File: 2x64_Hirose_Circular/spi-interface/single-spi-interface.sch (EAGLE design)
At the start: 53 parts, among them P1 BLUE, P2 BLUE, P3 BLUE, P4 BLUE, P5 BLUE, Q1 BC817, Q2 BC817

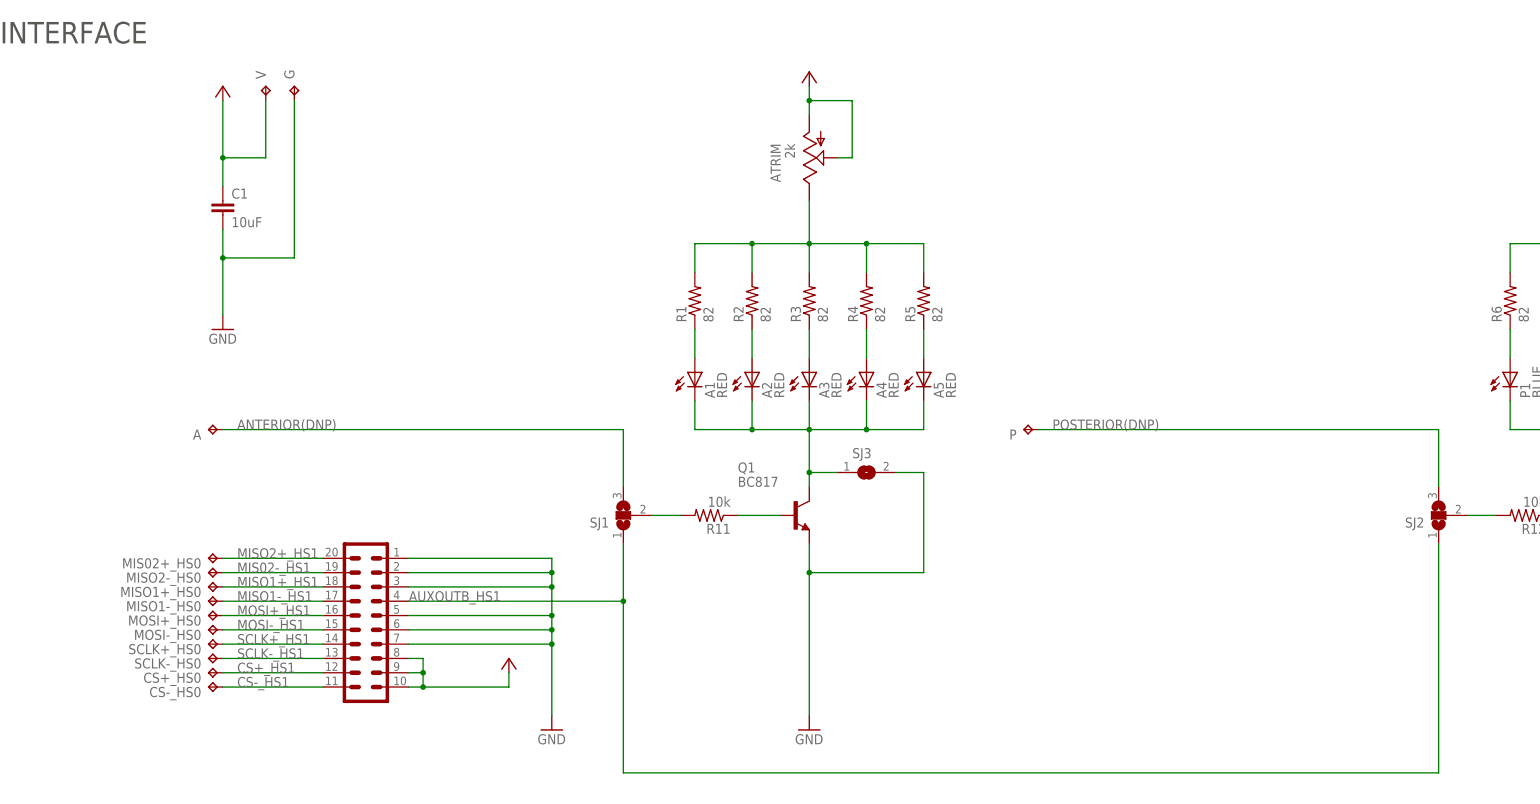
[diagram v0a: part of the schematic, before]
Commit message: Minor mods to headstage. Started routing the SPI interface.
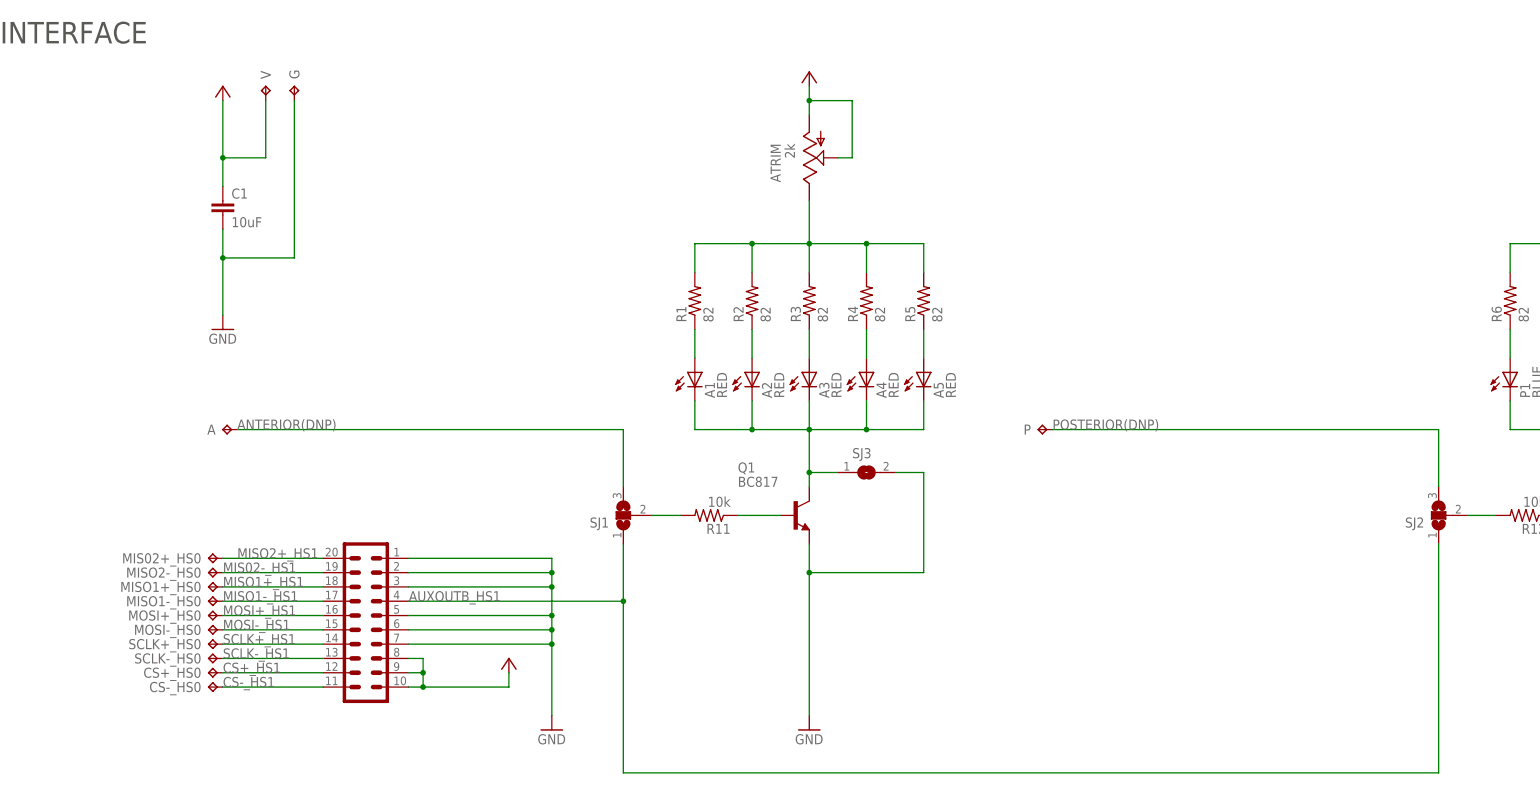
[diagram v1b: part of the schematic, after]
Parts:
- A, CS+_HS0, CS-_HS0, MIS02+_HS0, MISO1+_HS0, MISO1-_HS0, MISO2-_HS0, MOSI+_HS0, MOSI-_HS0, P, SCLK+_HS0, SCLK-_HS0: value TP_01 -> TP_SPI_WIRE; device headstage:TP_01 -> jonnew:TP_SPI_WIRE
- G, V: value TP_02 -> TP_SPI_WIRE; device headstage:TP_02 -> jonnew:TP_SPI_WIRE
- renumbered HS1 to DIO_HS0
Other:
- moved on the sheet: A, P

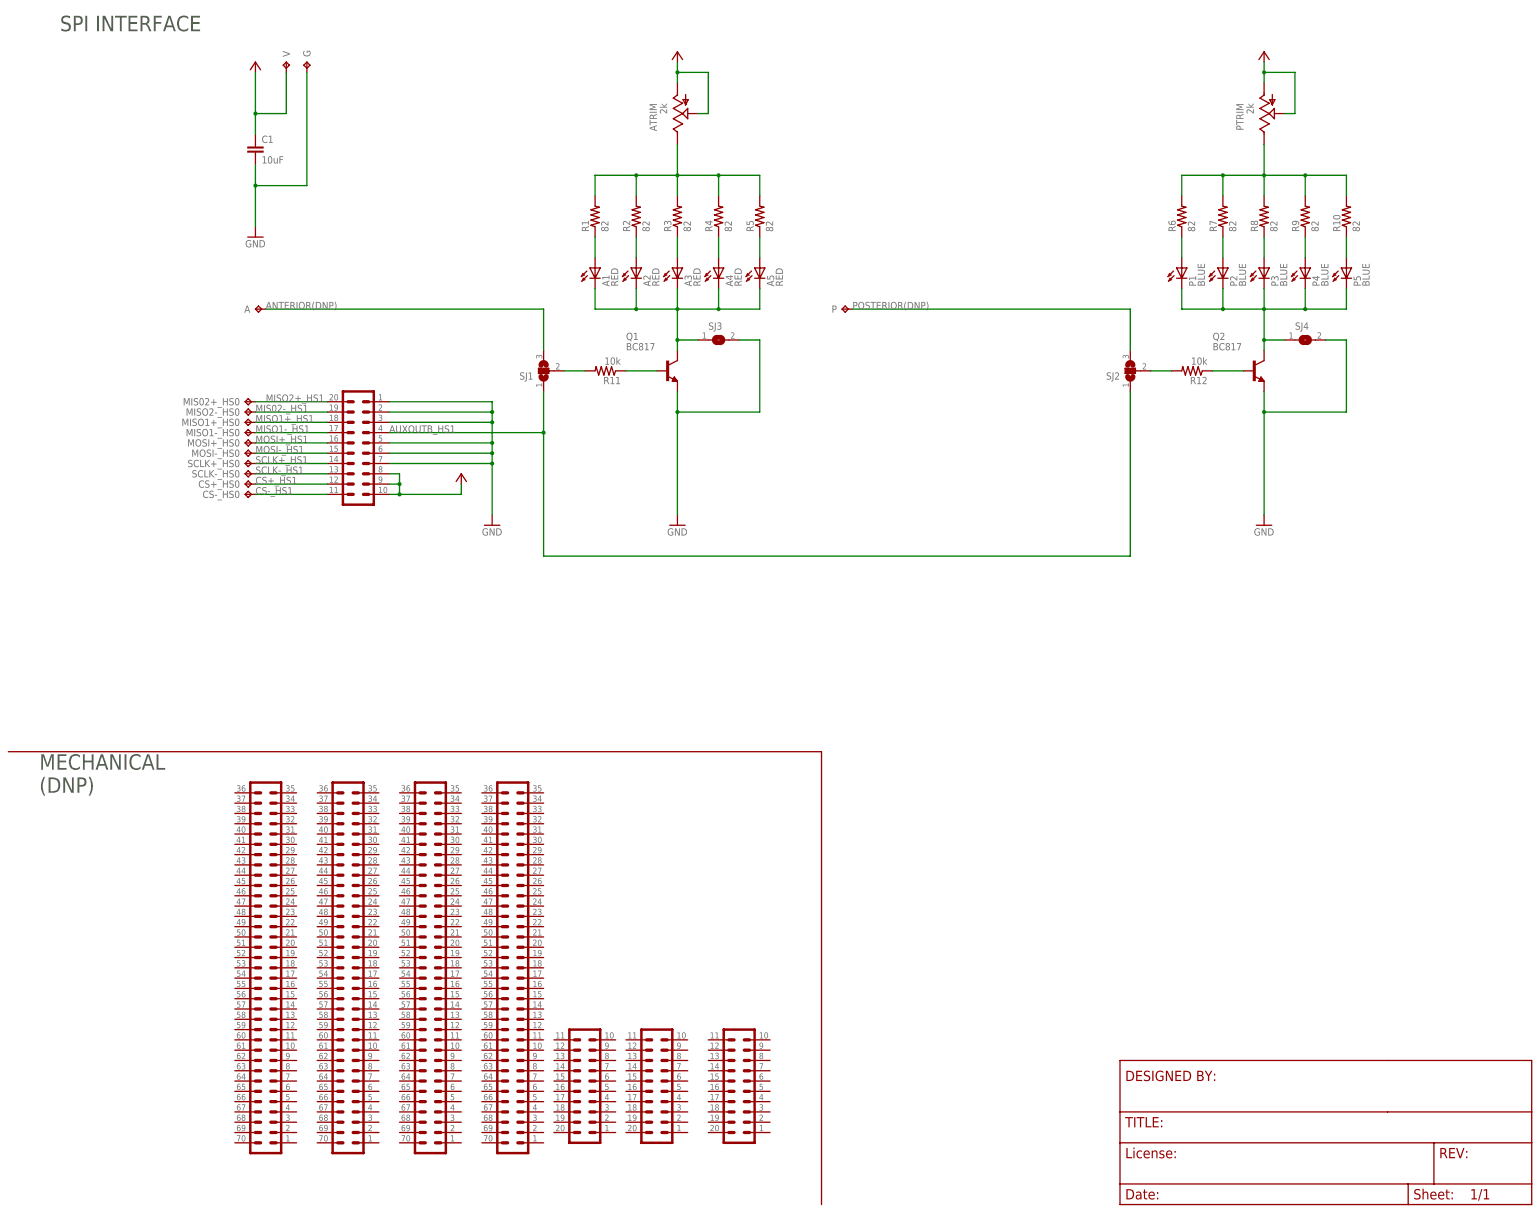
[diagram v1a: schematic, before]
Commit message: More updates to SPI interface board.
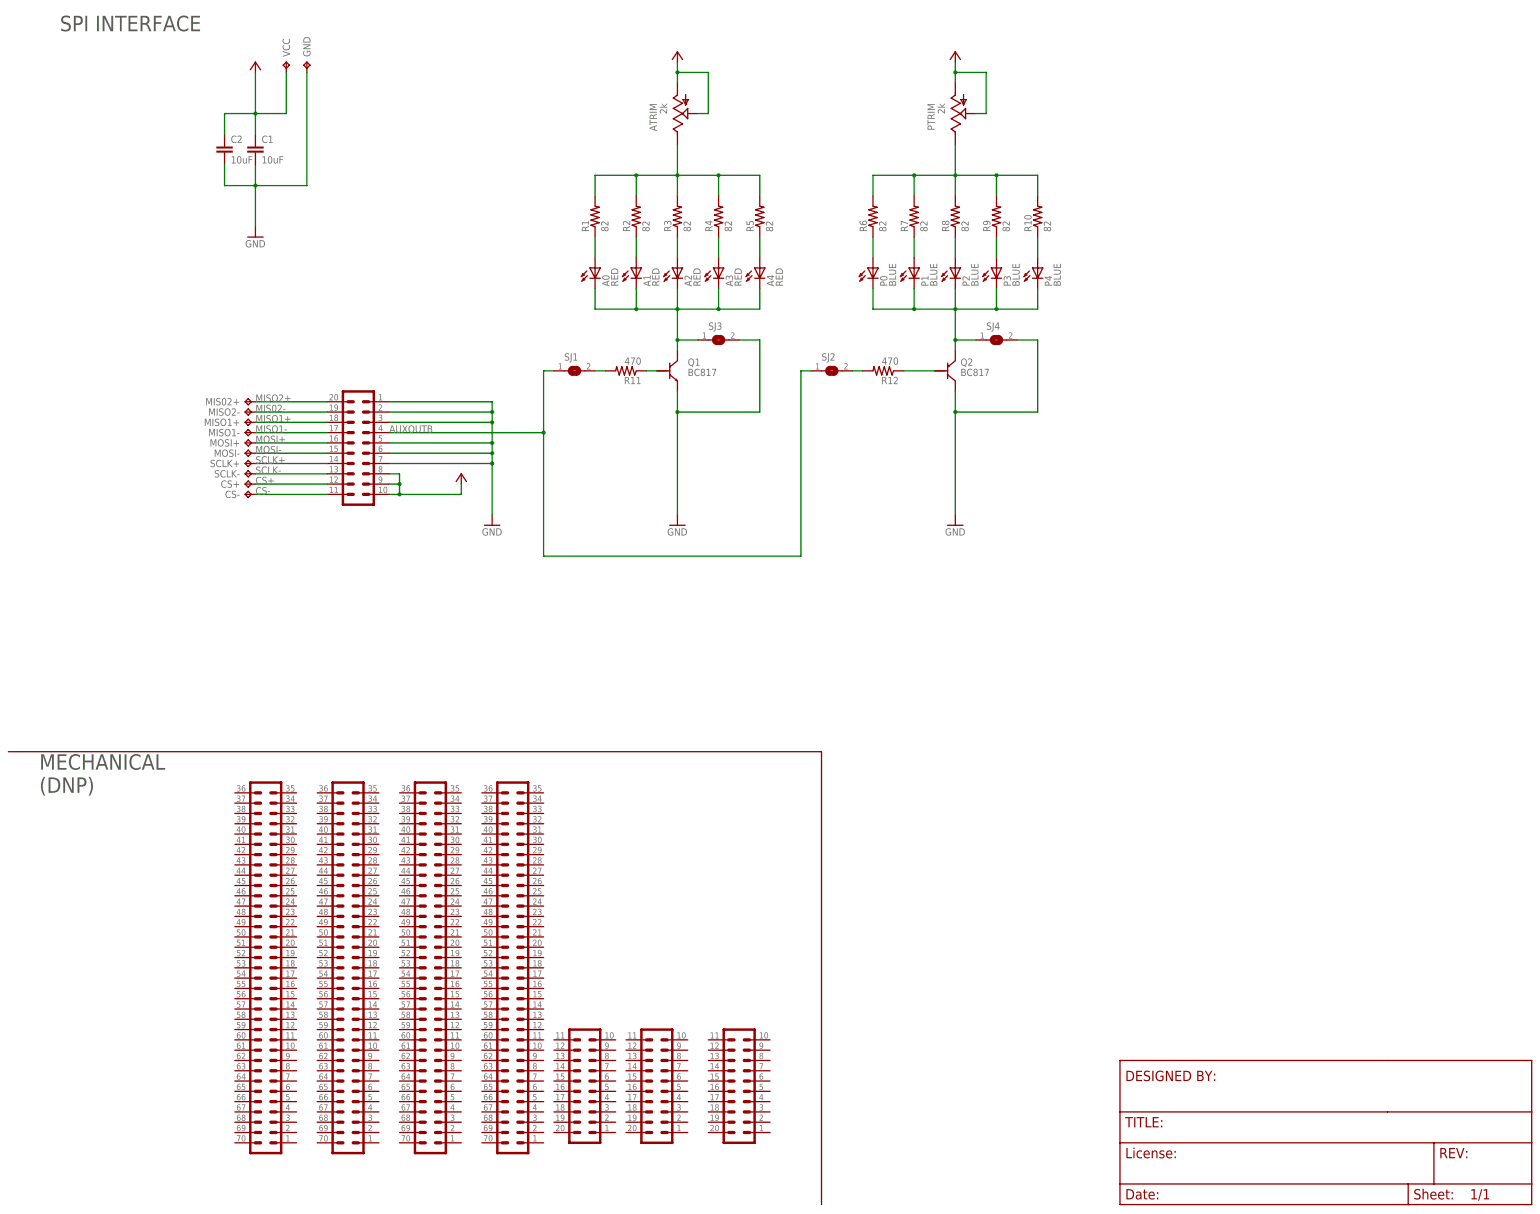
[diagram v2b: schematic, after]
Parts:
- removed A, P: TP_SPI_WIRE, jonnew:TP_SPI_WIRE
- removed A5: RED, cyclops:LED_0603
- removed P5: BLUE, cyclops:LED_0603
- added A0: RED, jonnew:LED_0402
- added C2: 10uF, headstage:C_0805
- added P0: BLUE, jonnew:LED_0402
- A1, A2, A3, A4, P1, P2, P3, P4: device cyclops:LED_0603 -> jonnew:LED_0402
- Q1: device cyclops:BC817-16SMD -> jonnew:NPN_SOT23-BEC
- Q2: device cyclops:BC817-16SMD -> jonnew:PNP_SOT23-BEC
- R1, R10, R2, R3, R4, R5, R6, R7, R8, R9: device headstage:R_0402 -> jonnew:R_0402
- R11, R12: value 10k -> 470
- SJ1, SJ2: device jumper:SJ2W -> jumper:SJ
- renumbered CS+_HS0 to CS+, CS-_HS0 to CS-, G to GND, MIS02+_HS0 to MIS02+, MISO1+_HS0 to MISO1+, MISO1-_HS0 to MISO1-, MISO2-_HS0 to MISO2-, MOSI+_HS0 to MOSI+, MOSI-_HS0 to MOSI-, SCLK+_HS0 to SCLK+, SCLK-_HS0 to SCLK-, V to VCC
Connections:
- net AUXOUTB_HS1 renamed AUXOUTB
- net CS+_HS1 renamed CS+
- net CS-_HS1 renamed CS-
- net MIS02-_HS1 renamed MIS02-
- net MISO1+_HS1 renamed MISO1+
- net MISO1-_HS1 renamed MISO1-
- net MISO2+_HS1 renamed MISO2+
- net MOSI+_HS1 renamed MOSI+
- net MOSI-_HS1 renamed MOSI-
- net SCLK+_HS1 renamed SCLK+
- net SCLK-_HS1 renamed SCLK-
- removed net ANTERIOR(DNP): A.TP, SJ1.3
- removed net POSTERIOR(DNP): P.TP, SJ2.3
- removed net VDD: ATRIM.A, ATRIM.S, C1.1, DIO_HS0.10, DIO_HS0.8, DIO_HS0.9, PTRIM.A, PTRIM.S, VCC.TP
- new net VCC: ATRIM.A, ATRIM.S, C1.1, C2.1, DIO_HS0.10, DIO_HS0.8, DIO_HS0.9, PTRIM.A, PTRIM.S, VCC.TP
- net B2: now also P0.C, Q2.E; no longer P5.C, Q2.C
- net F1: now also A0.C; no longer A5.C
- net GND: now also C2.2, Q2.C; no longer Q2.E
- net N$10: now also A3.A; no longer A4.A
- net N$11: now also P3.A, R9.1; no longer A5.A, R5.1
- net N$12: now also P1.A; no longer P2.A
- net N$13: now also P2.A; no longer P3.A
- net N$14: now also A4.A, R5.1; no longer P4.A, R9.1
- net N$15: now also P4.A; no longer P5.A
- net N$2: now also P0.A; no longer P1.A
- net N$3: now also A0.A; no longer A1.A
- net N$8: now also A1.A; no longer A2.A
- net N$9: now also A2.A; no longer A3.A
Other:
- moved on the sheet: A1, A2, A3, A4, P1, P2, P3, P4, PTRIM, R10, R11, R12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

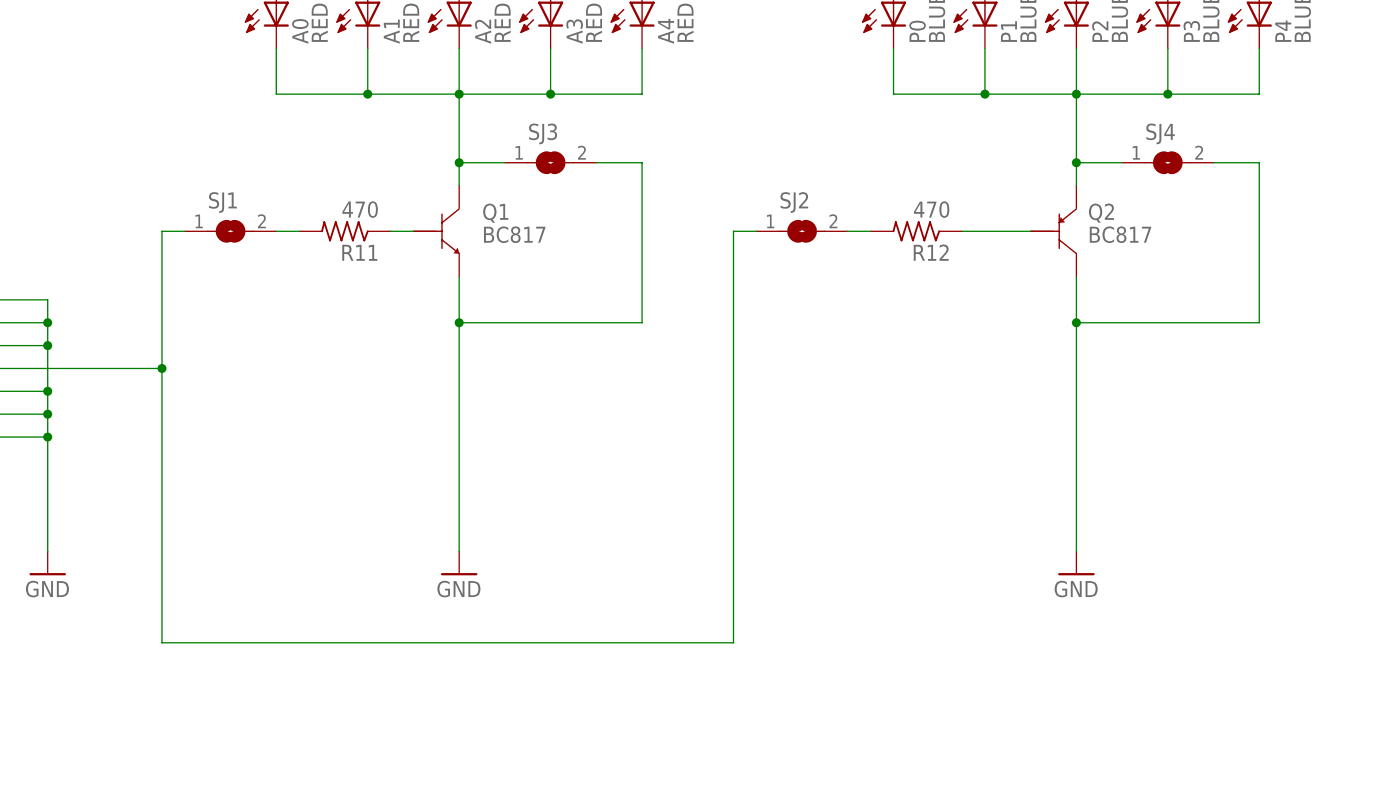
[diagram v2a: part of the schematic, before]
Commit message: Finished 128-channel spi interface. Time to fabricate mechanical mockups.
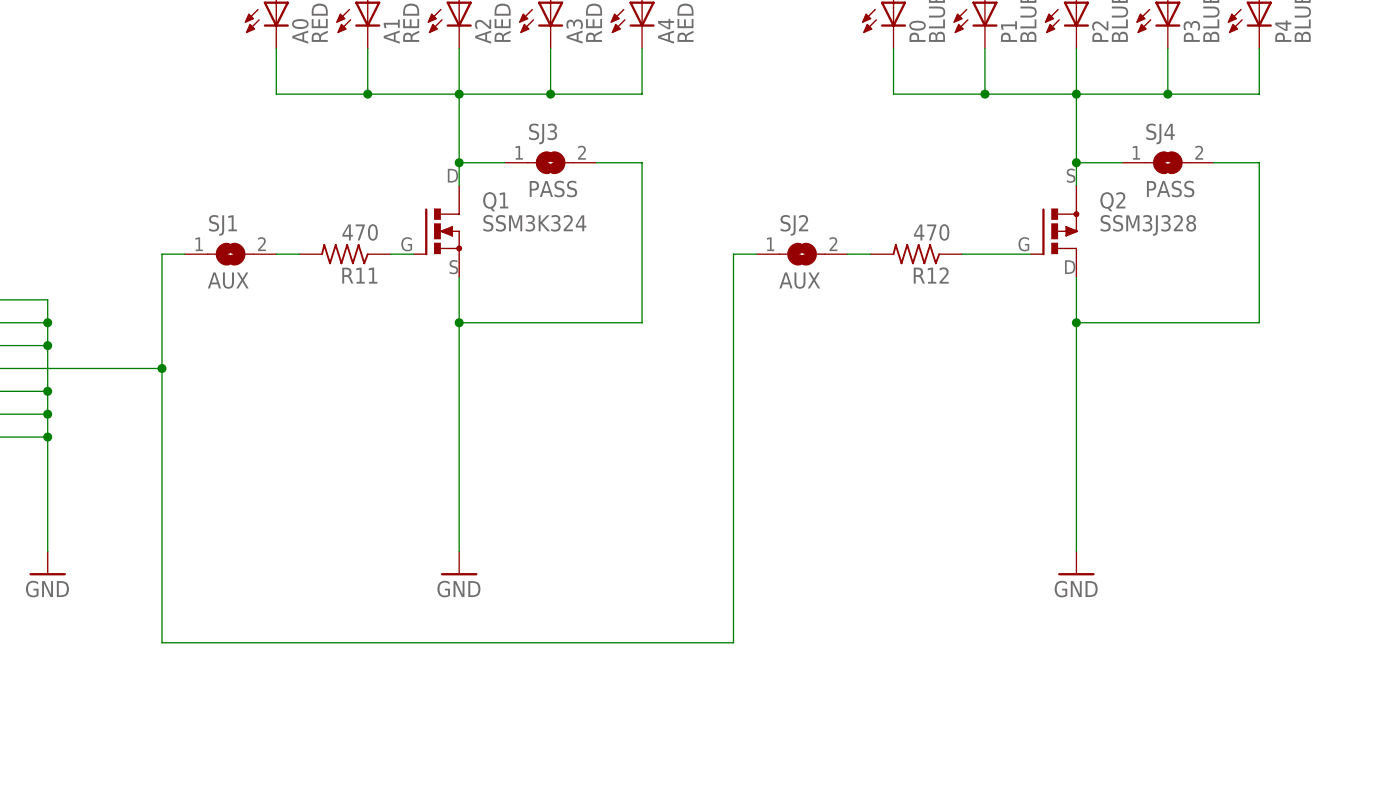
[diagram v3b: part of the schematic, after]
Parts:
- CS+, MIS02+, MISO1+, MOSI+, SCLK+, VCC: value TP_SPI_WIRE -> TP_SPI_WIRE+; device jonnew:TP_SPI_WIRE -> jonnew:TP_SPI_WIRE+
- CS-, GND, MISO1-, MISO2-, MOSI-, SCLK-: value TP_SPI_WIRE -> TP_SPI_WIRE-; device jonnew:TP_SPI_WIRE -> jonnew:TP_SPI_WIRE-
- DIO_E1B: value JMD20-V -> (none)
- Q1: value BC817 -> SSM3K324; device jonnew:NPN_SOT23-BEC -> jonnew:N-MOSFET_SOT23-GSD
- Q2: value BC817 -> SSM3J328; device jonnew:PNP_SOT23-BEC -> jonnew:P-MOSFET_SOT23-GSD
- SJ1, SJ2: value (none) -> AUX
- SJ3, SJ4: value (none) -> PASS
- renumbered DIO_HS0 to DIO_E1B, U$2 to MECH_N1B, U$3 to MECH_W1B, U$4 to MECH_E0B, U$5 to MECH_S0B, U$6 to MECH_W0B, U$7 to MECH_N0B, U$8 to MECH_S1B
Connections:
- net B2: now also Q2.S; no longer Q2.E
- net F1: now also Q1.D; no longer Q1.C
- net GND: now also Q1.S, Q2.D; no longer Q1.E, Q2.C
- net N$28: now also Q1.G; no longer Q1.B
- net N$5: now also Q2.G; no longer Q2.B
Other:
- moved on the sheet: R11, R12, SJ1, SJ2
